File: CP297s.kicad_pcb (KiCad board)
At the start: 2 copper layers, 155.1 x 156 mm, 128 parts, among them J1 Conn_01x05_Male, J2 Conn_01x04_Female, J3 pin header 01x15 2.54mm, J4 Conn_01x06_Female, J5 PG203J, J6 PG203J, J7 PG203J, J8 Conn_01x03_Female, K1 CONN_3, K2 CONN_3, K3 TK85_BUS, P2 CONN_2, P6 CONN_2, SW1 SW_SPDT, U1 Z80, U10 74LS125, U11 74LS393, U12 74LS574, U13 74LS08, U14 74LS251, U15 74HC86, U16 74LS245, U17 74LS32, U18 74HCT00, U19 74LS138, U2 62256, U20 74HC74, U21 74HC74, U22 74LS165, U23 74LS32, U24 AY-3-8910, U25 74LS08, U26 74LS138, U3 27256, U4 74HC04, U5 74HC74, U6 74LS393, U7 74LS11, U8 74LS32, U9 74LS245, X1 6.5MHz

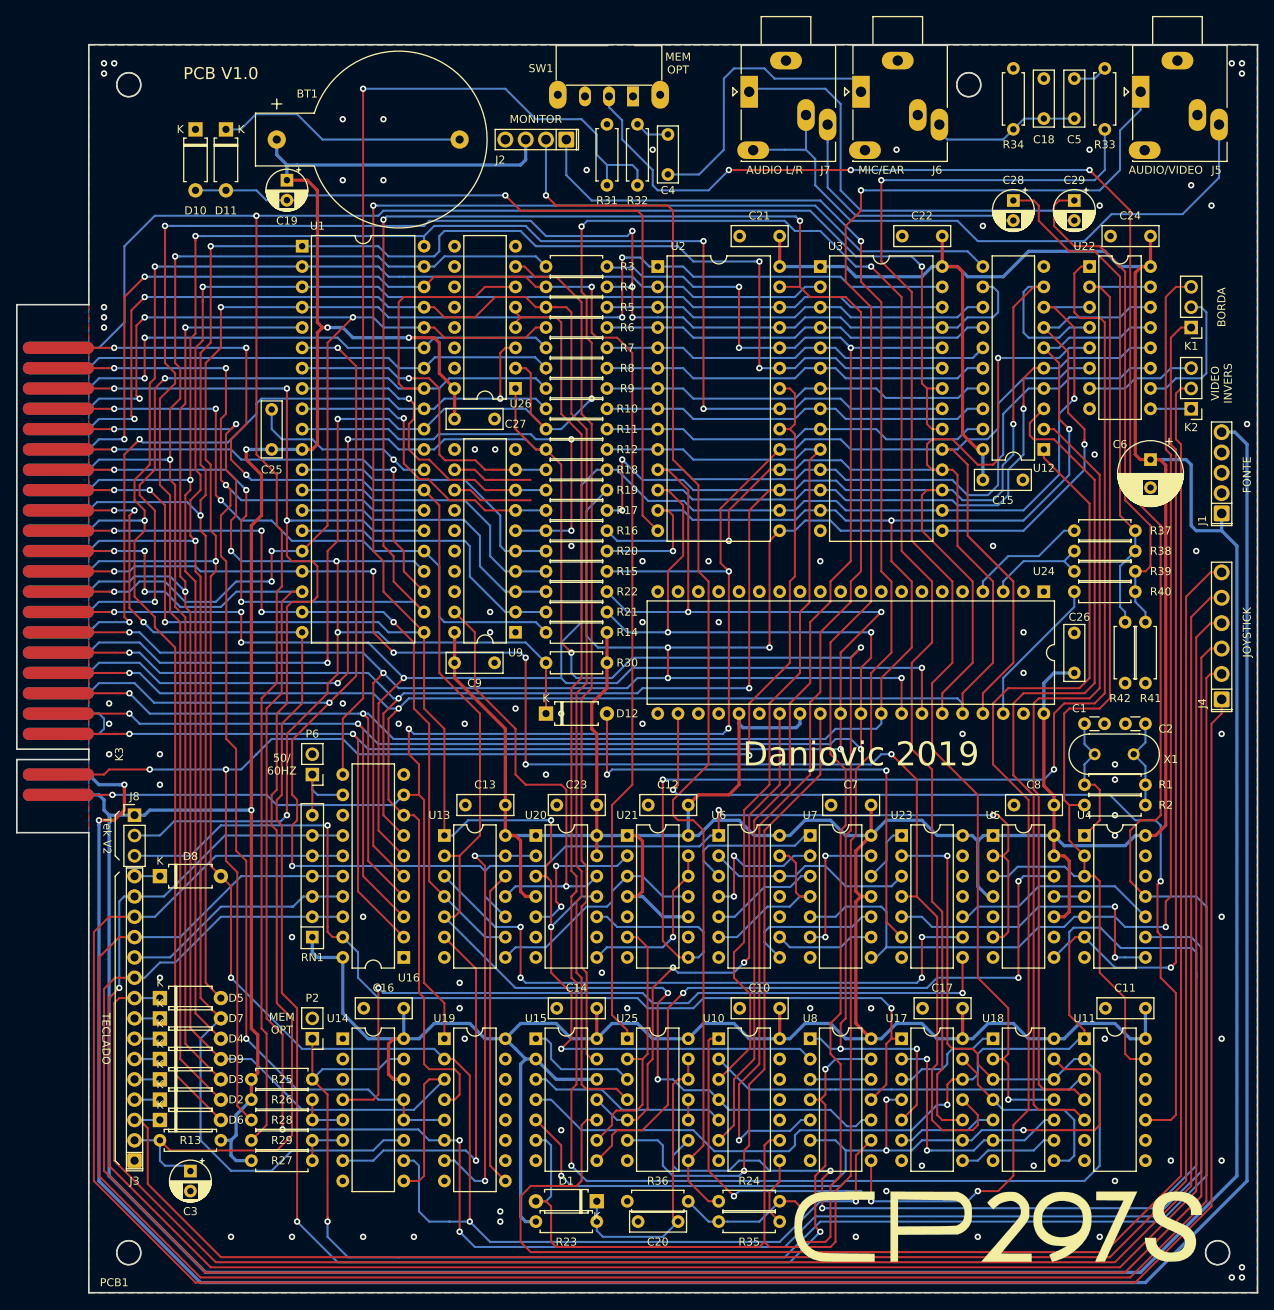
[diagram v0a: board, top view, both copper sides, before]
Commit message: Aesthetic improvement, gerbers added
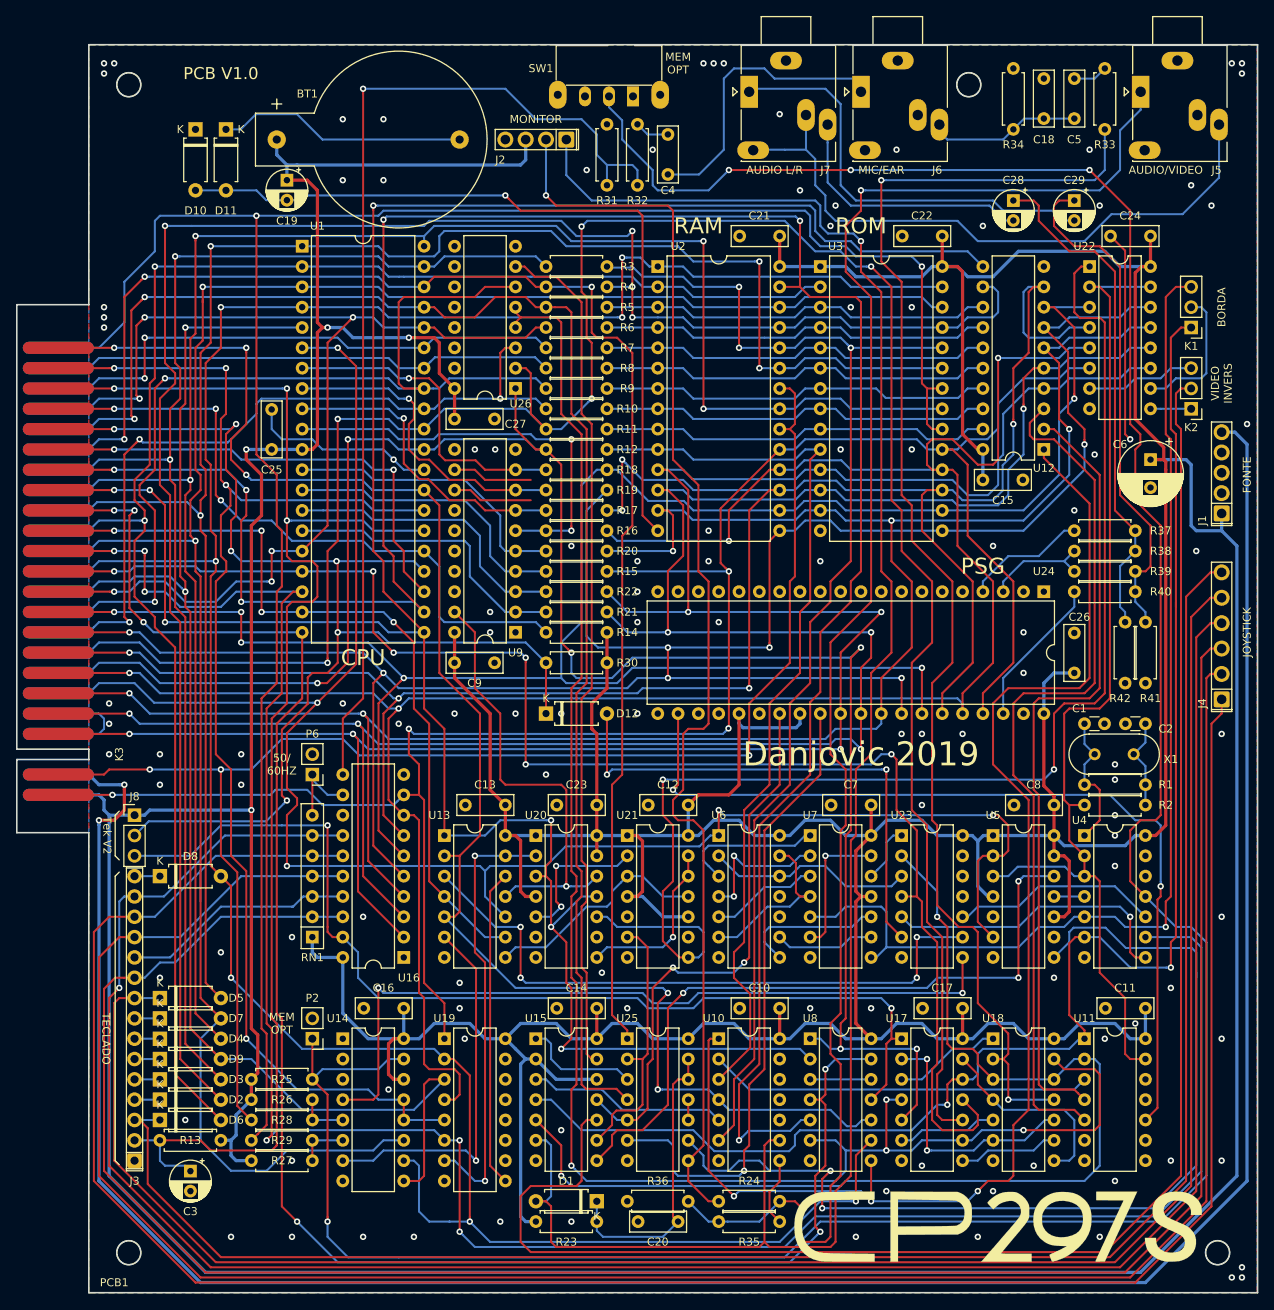
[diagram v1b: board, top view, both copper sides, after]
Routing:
- net GND: track 49.3 -> 75.7 mm, vias 88 -> 117
- net Net-(U25-Pad9): track 127.7 -> 123.9 mm
- net /1.625MHz: track 114.0 -> 110.2 mm
- net ~HALT: track 271.2 -> 274.5 mm
- net VSYNC: track 141.3 -> 138.7 mm
- net Net-(P2-Pad1): track 362.3 -> 360.2 mm
- net ~RESET: track 171.6 -> 169.7 mm
- net ~RD: track 304.6 -> 306.1 mm
- net NOP: track 55.2 -> 56.7 mm
- net ~CSYNC: track 242.4 -> 243.9 mm
- net ~M1: track 160.1 -> 161.2 mm
- net AUDIO-MONO: track 79.2 -> 80.3 mm
- net Net-(U23-Pad5): track 38.4 -> 37.3 mm, vias 2 -> 1
- net /RAW_VIDEO: track 157.0 -> 158.1 mm
- net ~ROMCS: track 262.7 -> 263.8 mm
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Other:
- board text added: "CPU"
- board text added: "PSG"
- board text added: "RAM"
- board text added: "ROM"
